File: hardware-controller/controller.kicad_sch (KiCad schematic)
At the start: 6 parts, among them J1 SENSOR_LINK_2mm, J4 USB_STACK_4_1.27mm, J5 USB2_PIGTAIL_4_WIRES, U2 ADS1115 module

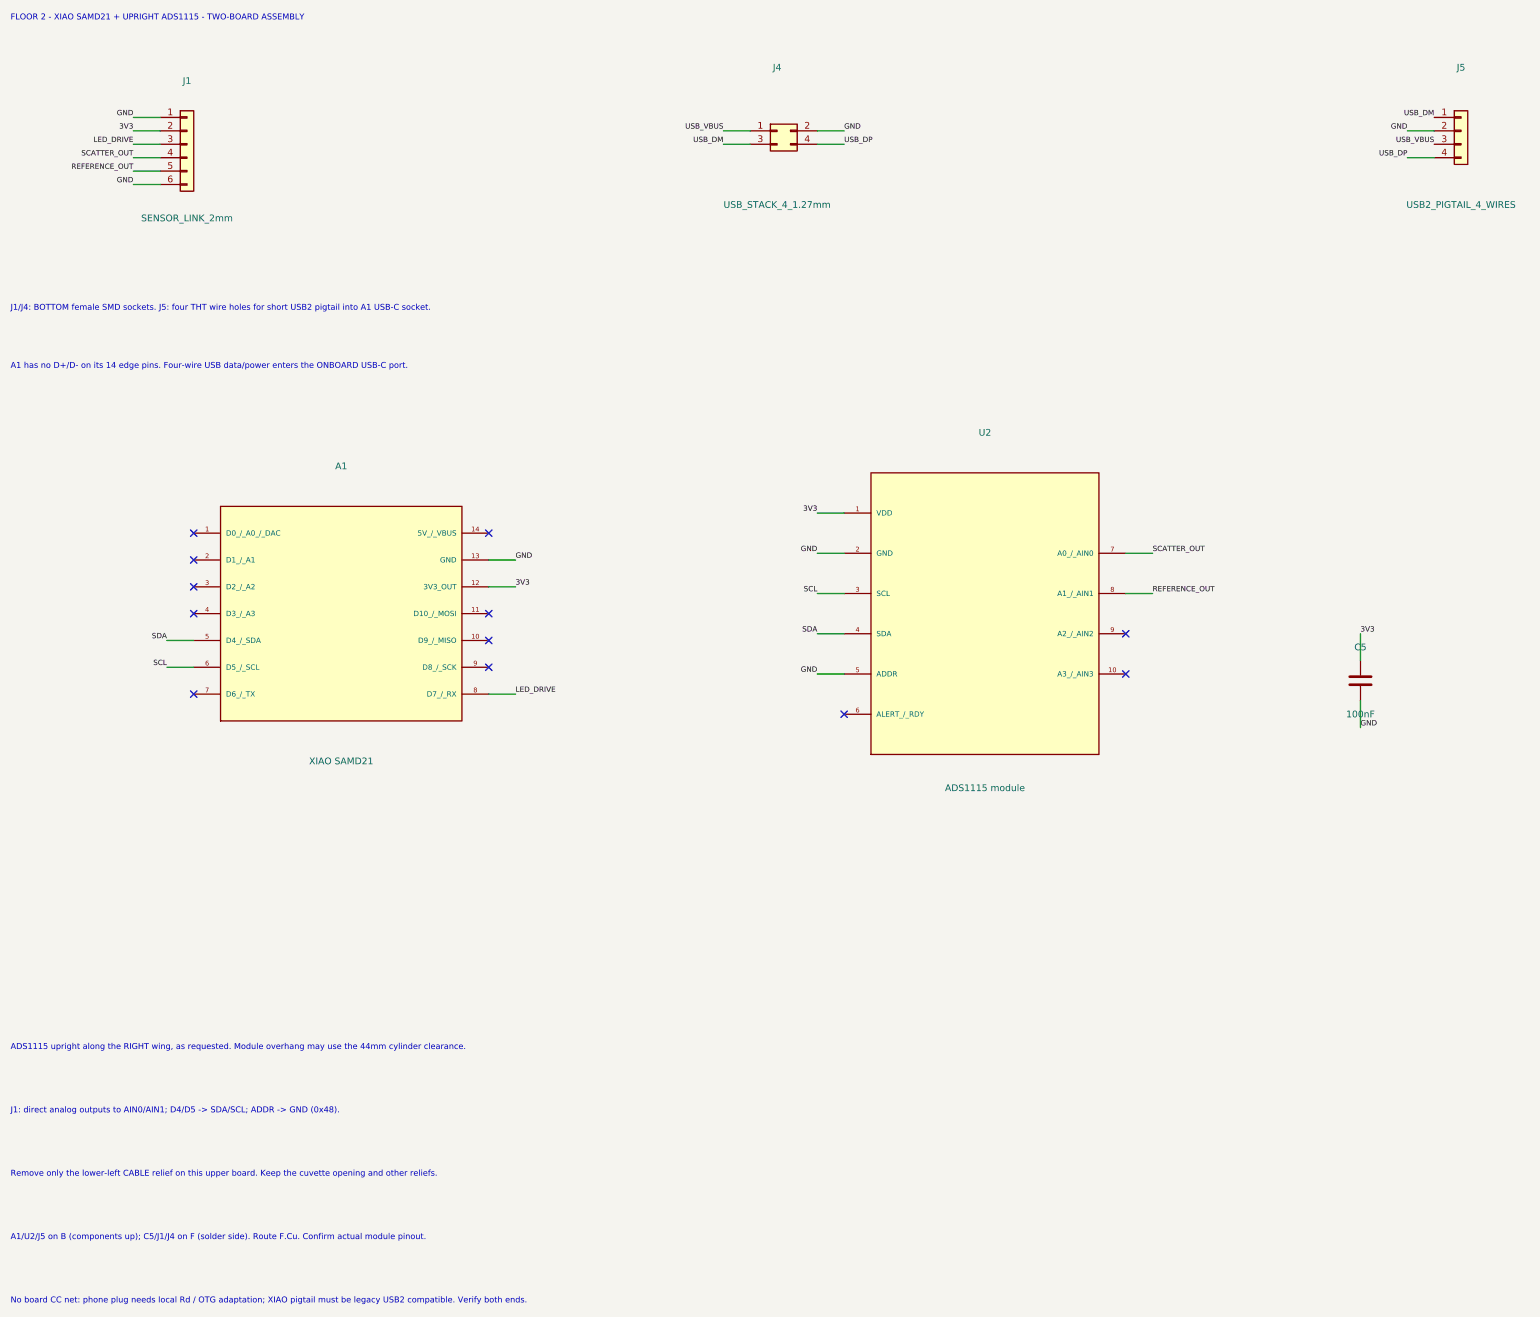
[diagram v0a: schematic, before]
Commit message: Organize project, add calibration app and record prototype bench results
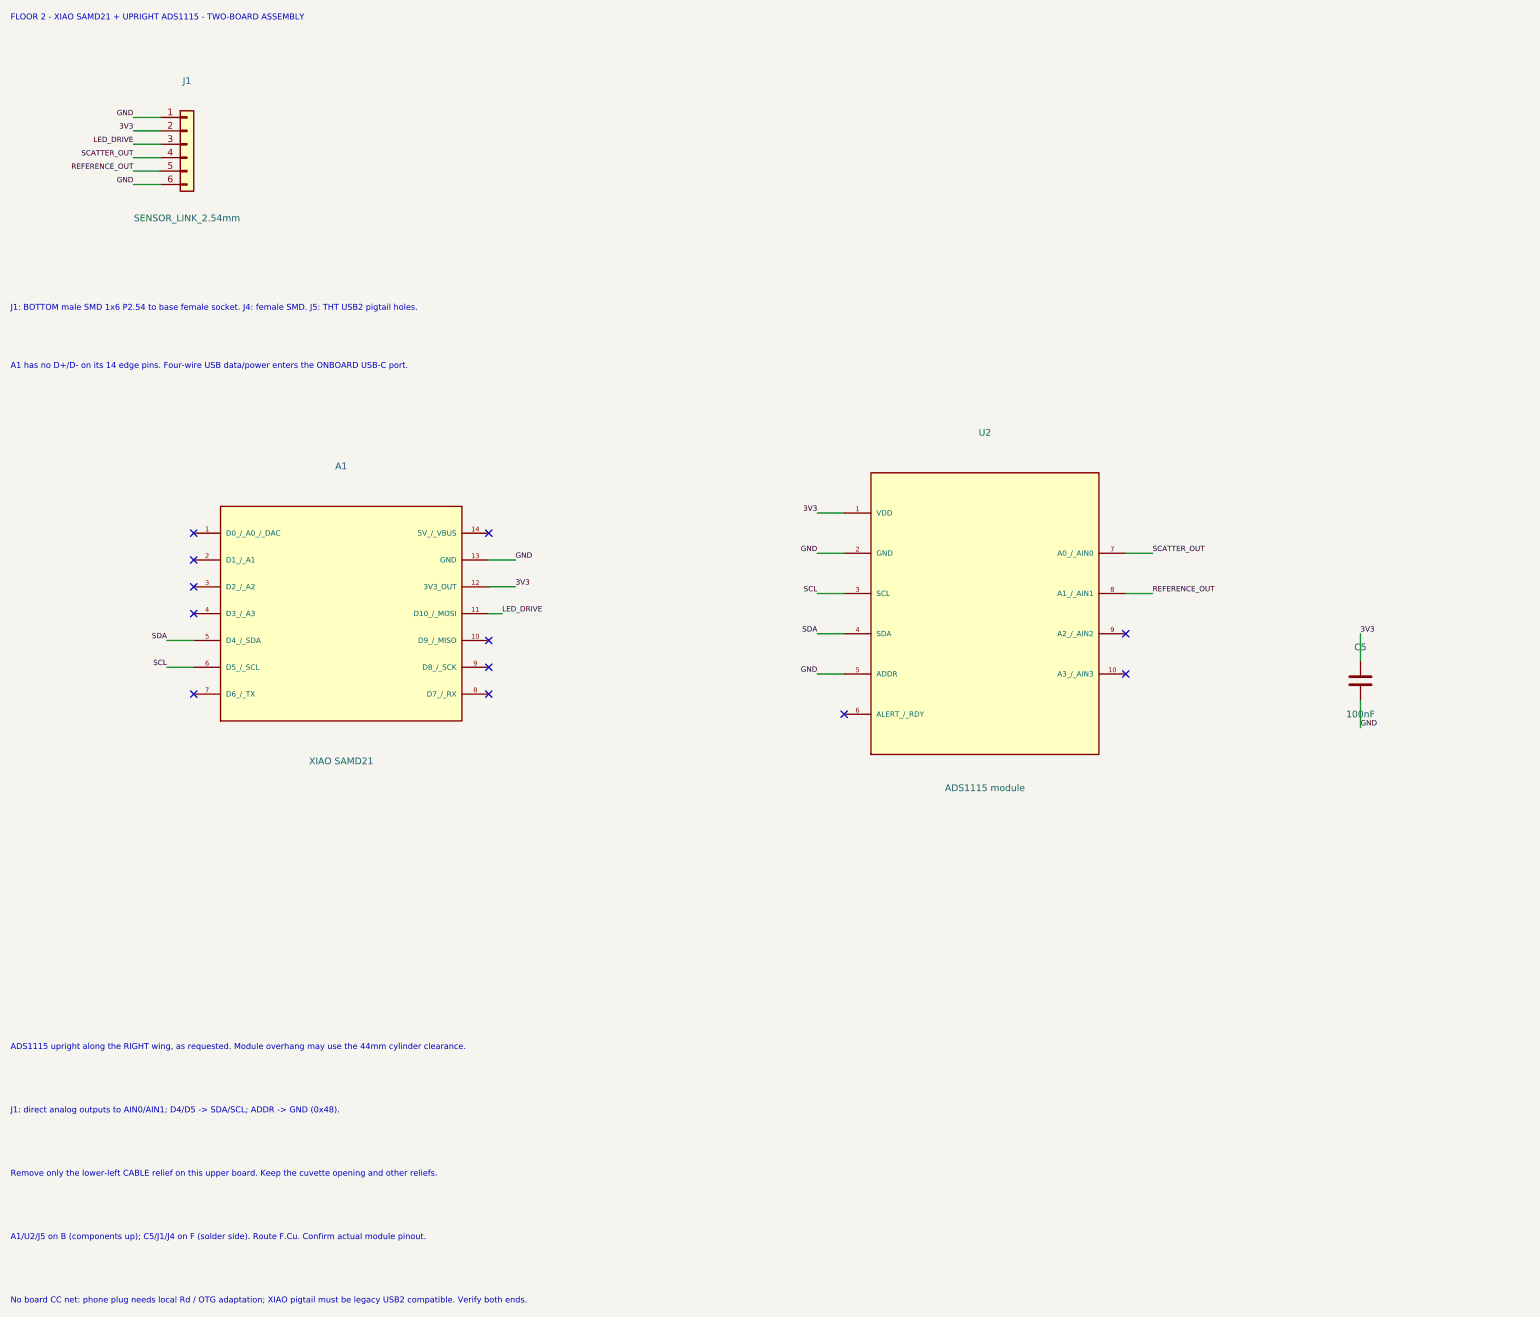
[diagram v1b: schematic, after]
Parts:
- removed J4: USB_STACK_4_1.27mm, Turbimeter:USB_StackSocket_2x02_P1.27mm_Upper_v10, symbol Connector_Generic:Conn_02x02_Odd_Even
- removed J5: USB2_PIGTAIL_4_WIRES, Turbimeter:USB_Cable_WireHoles_2x02_P2mm, symbol Connector_Generic:Conn_01x04
- C5: footprint Capacitor_SMD:C_1206_3216Metric -> Capacitor_THT:C_Disc_D5.0mm_W2.5mm_P2.50mm
- J1: value SENSOR_LINK_2mm -> SENSOR_LINK_2.54mm; footprint Connector_PinSocket_2.00mm:PinSocket_1x06_P2.00mm_Vertical_SMD_Pin1Right -> Connector_PinHeader_2.54mm:PinHeader_1x06_P2.54mm_Vertical_SMD_Pin1Right
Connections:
- net LED_DRIVE: now also A1.11 (D10_/_MOSI); no longer A1.8 (D7_/_RX)
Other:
- note added: "J1: BOTTOM male SMD 1x6 P2.54 to base female socket. J4: female SMD. J5: THT USB2 pigtail holes."
- note removed: "J1/J4: BOTTOM female SMD sockets. J5: four THT wire holes for short USB2 pigtail into A1 USB-C socket."
